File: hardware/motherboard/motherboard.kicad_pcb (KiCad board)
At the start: 2 copper layers, 83.7 x 56.7 mm, 55 parts, among them J1 Conn_01x02, J2 Conn_02x03_Odd_Even, J3 Conn_01x04, U1 ESP32-WROOM-32, U2 SHTC3, U3 BMP390, U4 TPS62177DQC, U8 NRF24L01_Breakout

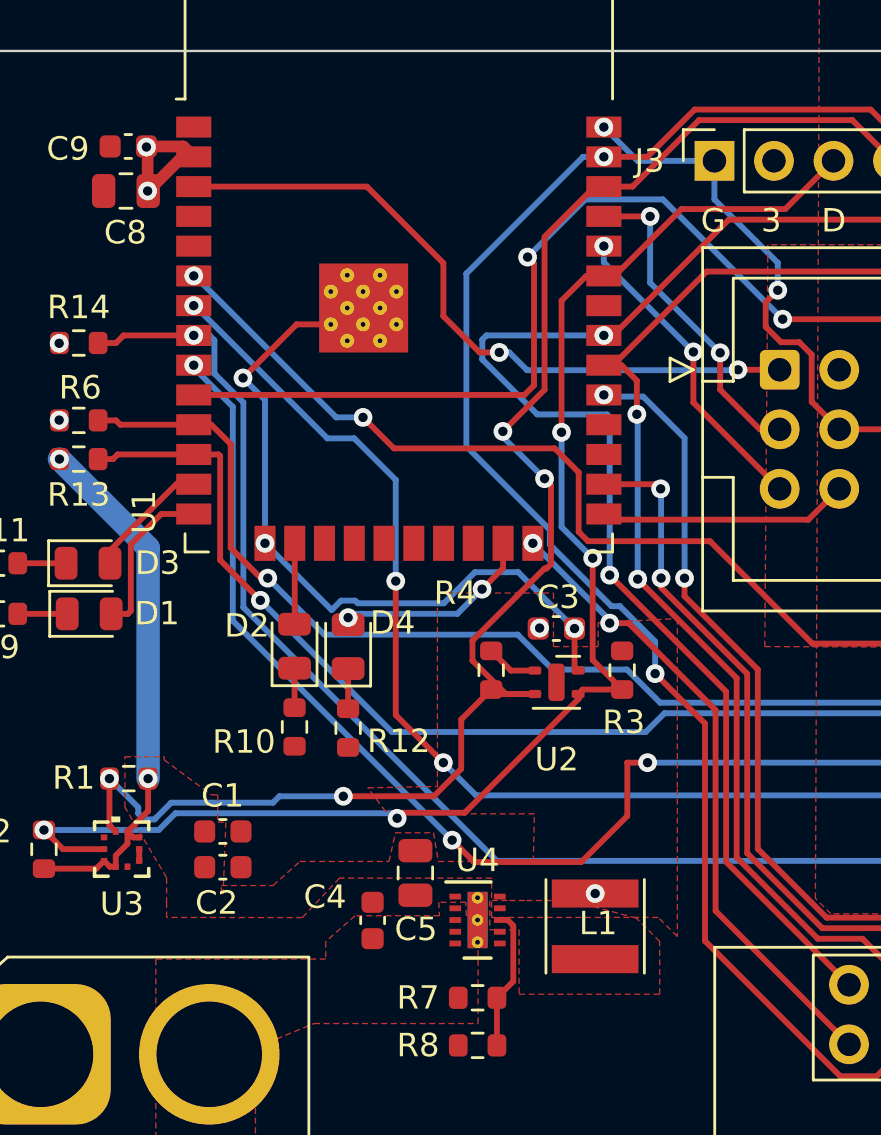
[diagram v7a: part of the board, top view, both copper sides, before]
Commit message: Fixed Clearance Issues
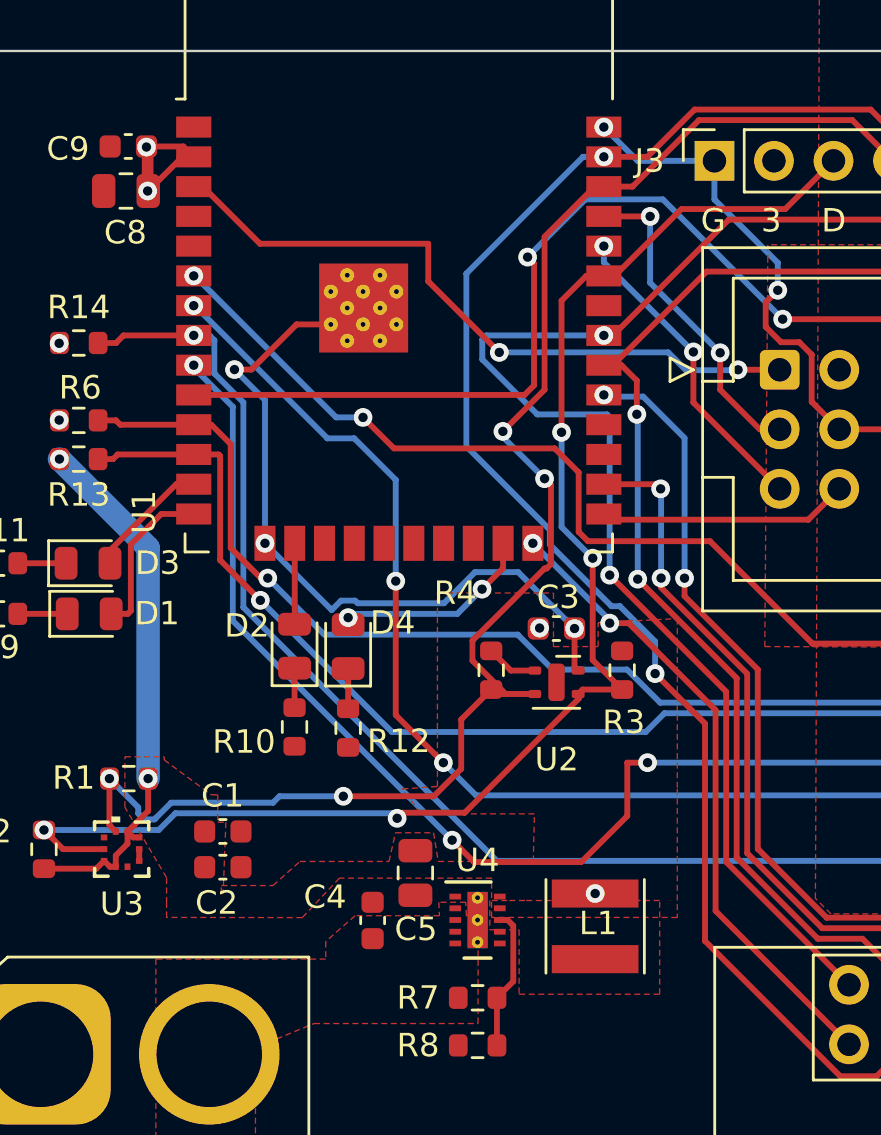
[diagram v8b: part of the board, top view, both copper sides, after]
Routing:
- net GND: track 63.4 -> 64.1 mm
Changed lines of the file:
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@@
   (segment (start 165.772 98.978) (end 165.772 100.022) (width 0.25) (layer "F.Cu") (net 1))
   (segment (start 148.5918 99.917874) (end 148.6168 99.917874) (width 0.25) (layer "F.Cu") (net 1))
-  (segment (start 145.756071 99.917874) (end 143.470173 102.203772) (width 0.25) (layer "F.Cu") (net 1))
+  (segment (start 143.10531 101.84469) (end 143.829255 101.84469) (width 0.25) (layer "F.Cu") (net 1))
   (segment (start 147.9168 97.817874) (end 147.2168 98.517874) (width 0.25) (layer "F.Cu") (net 1))
   (segment (start 147.2168 99.917874) (end 147.9168 100.617874) (width 0.25) (layer "F.Cu") (net 1))
+  (segment (start 143.829255 101.84469) (end 145.756071 99.917874) (width 0.25) (layer "F.Cu") (net 1))
   (segment (start 157.616 114.535) (end 157.77 114.689) (width 0.25) (layer "F.Cu") (net 1))
   (segment (start 166.288299 98.461701) (end 165.772 98.978) (width 0.25) (layer "F.Cu") (net 1))
@@
   (segment (start 167.735 101.205826) (end 167.735 103.219) (width 0.25) (layer "F.Cu") (net 1))
   (segment (start 166.429 100.679) (end 167.208174 100.679) (width 0.25) (layer "F.Cu") (net 1))
-  (segment (start 147.2168 99.917874) (end 145.756071 99.917874) (width 0.25) (layer "F.Cu") (net 1))
+  (segment (start 145.756071 99.917874) (end 147.2168 99.917874) (width 0.25) (layer "F.Cu") (net 1))
   (segment (start 167.208174 100.679) (end 167.735 101.205826) (width 0.25) (layer "F.Cu") (net 1))
   (segment (start 165.772 100.022) (end 166.429 100.679) (width 0.25) (layer "F.Cu") (net 1))
@@
   (via (at 158.8668 91.497874) (size 0.8) (drill 0.4) (layers "F.Cu" "B.Cu") (net 1))
   (via (at 166.288299 98.461701) (size 0.8) (drill 0.4) (layers "F.Cu" "B.Cu") (net 1))
-  (via (at 143.470173 102.203772) (size 0.8) (drill 0.4) (layers "F.Cu" "B.Cu") (net 1))
+  (via (at 143.10531 101.84469) (size 0.8) (drill 0.4) (layers "F.Cu" "B.Cu") (net 1))
   (via (at 144.4068 109.257874) (size 0.8) (drill 0.4) (layers "F.Cu" "B.Cu") (net 1))
-  (segment (start 144.4068 103.140399) (end 144.4068 109.257874) (width 0.25) (layer "B.Cu") (net 1))
+  (segment (start 144.4068 103.14618) (end 144.4068 109.257874) (width 0.25) (layer "B.Cu") (net 1))
   (segment (start 152.041195 111.818) (end 148.368805 111.818) (width 0.25) (layer "B.Cu") (net 1))
   (segment (start 148.368805 111.818) (end 148.255305 111.7045) (width 0.25) (layer "B.Cu") (net 1))
+  (segment (start 143.10531 101.84469) (end 144.4068 103.14618) (width 0.25) (layer "B.Cu") (net 1))
   (segment (start 155.2105 110.4895) (end 153.369695 110.4895) (width 0.25) (layer "B.Cu") (net 1))
-  (segment (start 143.470173 102.203772) (end 144.4068 103.140399) (width 0.25) (layer "B.Cu") (net 1))
   (segment (start 166.288299 97.288299) (end 166.288299 98.461701) (width 0.25) (layer "B.Cu") (net 1))
   (segment (start 166.288299 97.288299) (end 163.586 94.586) (width 0.25) (layer "B.Cu") (net 1))
@@
   (segment (start 147.25406 112.105134) (end 144.4068 109.257874) (width 0.25) (layer "B.Cu") (net 1))
   (segment (start 153.369695 110.4895) (end 152.041195 111.818) (width 0.25) (layer "B.Cu") (net 1))
-  (segment (start 148.758377 94.037874) (end 141.3668 94.037874) (width 0.25) (layer "F.Cu") (net 2))
-  (segment (start 154.405114 101.112374) (end 153.563374 101.112374) (width 0.25) (layer "F.Cu") (net 2))
+  (segment (start 141.75642 94.037874) (end 141.3668 94.037874) (width 0.25) (layer "F.Cu") (net 2))
+  (segment (start 144.193546 96.475) (end 141.75642 94.037874) (width 0.25) (layer "F.Cu") (net 2))
   (segment (start 166.37 101.854) (end 164.592 101.854) (width 0.25) (layer "F.Cu") (net 2))
-  (segment (start 152.019 99.568) (end 152.019 97.298497) (width 0.25) (layer "F.Cu") (net 2))
-  (segment (start 153.563374 101.112374) (end 152.019 99.568) (width 0.25) (layer "F.Cu") (net 2))
-  (segment (start 152.019 97.298497) (end 148.758377 94.037874) (width 0.25) (layer "F.Cu") (net 2))
+  (segment (start 154.405114 101.112374) (end 151.375 98.08226) (width 0.25) (layer "F.Cu") (net 2))
+  (segment (start 151.375 96.475) (end 144.193546 96.475) (width 0.25) (layer "F.Cu") (net 2))
+  (segment (start 151.375 98.08226) (end 151.375 96.475) (width 0.25) (layer "F.Cu") (net 2))
   (via (at 154.405114 101.112374) (size 0.8) (drill 0.4) (layers "F.Cu" "B.Cu") (net 2))
   (via (at 164.592 101.854) (size 0.8) (drill 0.4) (layers "F.Cu" "B.Cu") (net 2))
-  (segment (start 155.591497 101.870497) (end 164.575503 101.870497) (width 0.25) (layer "B.Cu") (net 2))
-  (segment (start 154.833374 101.112374) (end 155.591497 101.870497) (width 0.25) (layer "B.Cu") (net 2))
-  (segment (start 154.405114 101.112374) (end 154.833374 101.112374) (width 0.25) (layer "B.Cu") (net 2))
+  (segment (start 161.612374 101.112374) (end 162.370497 101.870497) (width 0.25) (layer "B.Cu") (net 2))
+  (segment (start 162.370497 101.870497) (end 164.575503 101.870497) (width 0.25) (layer "B.Cu") (net 2))
+  (segment (start 154.405114 101.112374) (end 161.612374 101.112374) (width 0.25) (layer "B.Cu") (net 2))
   (segment (start 164.575503 101.870497) (end 164.592 101.854) (width 0.25) (layer "B.Cu") (net 2))
   (segment (start 139.4 92.4) (end 139.35 92.35) (width 0.25) (layer "F.Cu") (net 3))
   (segment (start 159.695 113.848) (end 159.766 113.919) (width 0.25) (layer "F.Cu") (net 3))
   (segment (start 134.9756 123.141748) (end 137.208252 123.141748) (width 0.25) (layer "F.Cu") (net 3))
-  (segment (start 140.923926 92.325) (end 141.3668 92.767874) (width 0.5) (layer "F.Cu") (net 3))
+  (segment (start 140.923926 92.325) (end 141.3668 92.767874) (width 0.25) (layer "F.Cu") (net 3))
   (segment (start 135.637 100.711) (end 135.614 100.711) (width 0.25) (layer "F.Cu") (net 3))
   (segment (start 138.040237 122.581917) (end 138.040237 123.058174) (width 0.25) (layer "F.Cu") (net 3))
@@
   (segment (start 138.040237 123.058174) (end 137.790174 123.058174) (width 0.25) (layer "F.Cu") (net 3))
   (segment (start 138.540363 121.559574) (end 138.540363 122.081791) (width 0.25) (layer "F.Cu") (net 3))
-  (segment (start 139.35 92.325) (end 140.923926 92.325) (width 0.5) (layer "F.Cu") (net 3))
+  (segment (start 139.35 92.325) (end 140.923926 92.325) (width 0.25) (layer "F.Cu") (net 3))
   (segment (start 156.105 112.895) (end 156.125 112.875) (width 0.25) (layer "F.Cu") (net 3))
   (segment (start 135.614 100.711) (end 135.6 100.725) (width 0.25) (layer "F.Cu") (net 3))
@@
   (segment (start 140.882126 92.767874) (end 141.3668 92.767874) (width 0.5) (layer "F.Cu") (net 3))
   (segment (start 139.0396 121.808748) (end 138.789537 121.808748) (width 0.25) (layer "F.Cu") (net 3))
-  (segment (start 139.425 94.225) (end 140.882126 92.767874) (width 0.5) (layer "F.Cu") (net 3))
+  (segment (start 139.425 94.225) (end 140.882126 92.767874) (width 0.25) (layer "F.Cu") (net 3))
   (segment (start 158.366 124.333) (end 158.496 124.203) (width 0.25) (layer "F.Cu") (net 3))
   (segment (start 139.4196 119.298748) (end 139.4196 120.680337) (width 0.25) (layer "F.Cu") (net 3))
@@
     (polygon
       (pts
-        (xy 161.25 126.25)
-        (xy 160.25 125.25)
+        (xy 161.25 124.5)
+        (xy 160.225 124.5)
         (xy 157.45 124.5)
         (xy 155.5 124.5)
@@
         (xy 162.0012 112.4712)
         (xy 162.0012 119.7356)
-        (xy 162.0012 126.0348)
+        (xy 162 125.225)
         (xy 161.1884 125.222)
         (xy 154.0764 125.222)
@@
         (xy 151.2824 120.8024)
         (xy 151.2824 120.827113)
-        (xy 149.5552 120.7008)
-        (xy 148.7932 119.692118)
+        (xy 151.0302 120.7508)
+        (xy 150.2682 119.742118)
         (xy 151.765 119.634)
         (xy 151.765 111.379)
